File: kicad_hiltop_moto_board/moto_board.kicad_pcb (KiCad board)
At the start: 4 copper layers, 159.9 x 99.9 mm, 204 parts, among them J1 Conn_01x04, J10 Conn_01x01, J11 Conn_01x01, J12 Conn_01x03, J13 Conn_01x03, J2 Conn_01x04, J3 Conn_03x32_DIN41612, J4 Conn_01x04, J5 Conn_02x05_Top_Bottom, J6 Conn_01x01, J7 Conn_01x01, J8 Conn_01x03, J9 Conn_01x03, Q1 CSD18540Q5B, Q2 CSD18540Q5B, Q3 CSD18540Q5B, Q4 CSD18540Q5B, Q5 CSD18540Q5B, Q6 CSD18540Q5B, Q7 CSD18540Q5B, Q8 CSD18540Q5B, SW1 SW_Push, U1 DRV8704, U13 CP2102N-A01-GQFN24, U2 LD1117S33TR_SOT223, U22 STM32F072RBTx, U27 USB2502, U3 AT25DN512CSSHF-B, U7 DNF, Y1 50ppm 24.000MHZ, Y2 8MHZ, Y3 ABS25-32.768KHZ-6-T

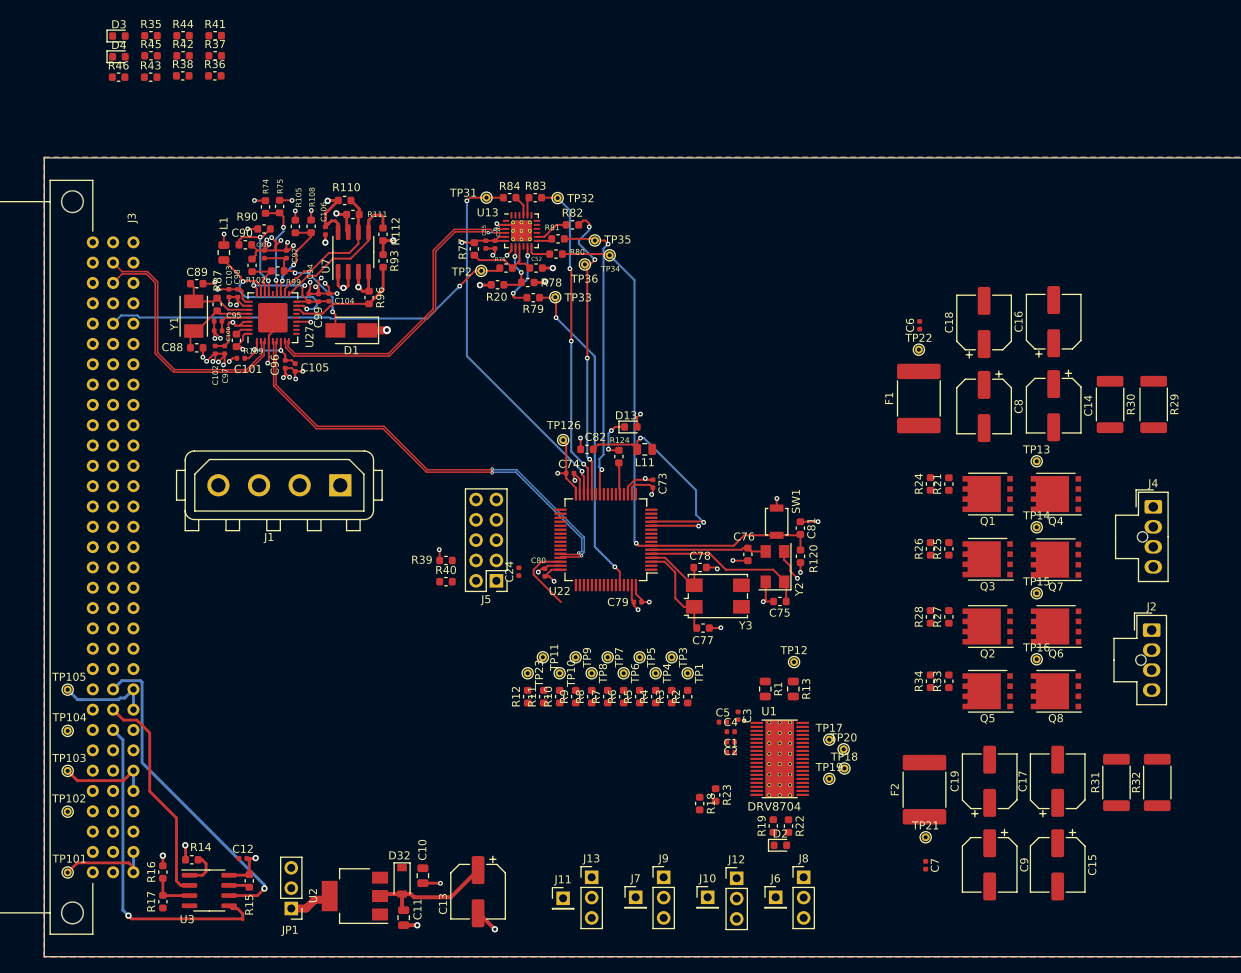
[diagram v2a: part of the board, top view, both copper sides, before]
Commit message: Updated moto board schematic and layout
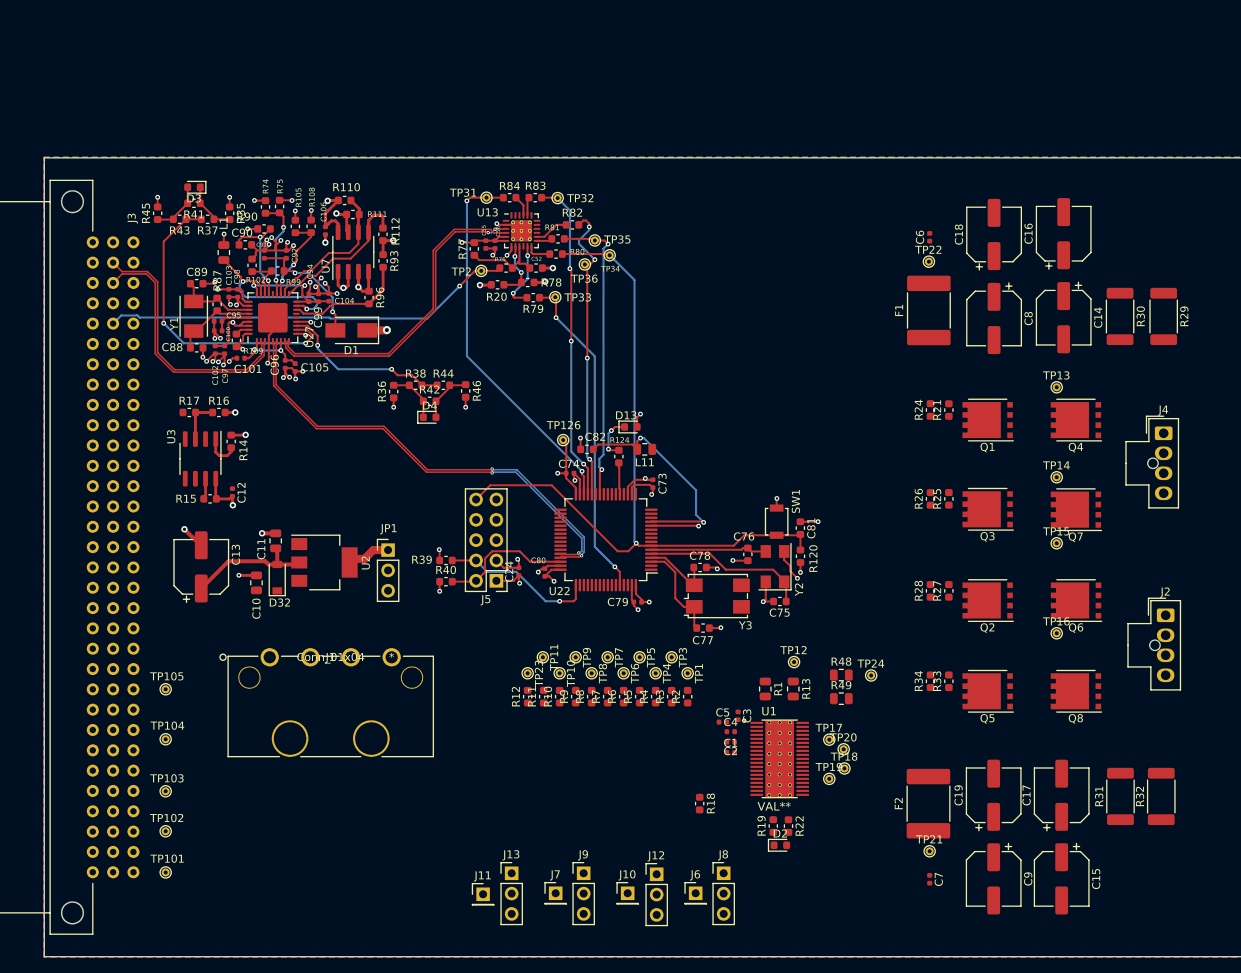
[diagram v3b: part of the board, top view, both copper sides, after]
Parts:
- removed R23: 10K, Resistor_SMD:R_0603_1608Metric
- added R48: DNF, Resistor_SMD:R_0805_2012Metric, F.Cu at (154.7, 109.7)
- added R49: 0R, Resistor_SMD:R_0805_2012Metric, F.Cu at (154.7, 112.7)
- added TP24: Test_Point, TestPoint:TestPoint_THTPad_D1.0mm_Drill0.5mm, F.Cu at (158.4, 109.8)
- J1: footprint Connector_TE-Connectivity:TE_MATE-N-LOK_350211-1_1x04_P5.08mm_Vertical -> Devtank_PCB_Lib:Molex_8981
- U1: value DRV8704 -> VAL**
- moved R17 61.2 mm to (73.2, 76.9), turned to 0 degrees
- moved D4 59.5 mm to (103.2, 77.5)
- moved R46 58.5 mm to (107.8, 74.2), turned to 270 degrees
- moved R16 57.9 mm to (76.9, 76.9), turned to 0 degrees
- moved R44 54.5 mm to (105.0, 73.5)
- moved U3 54.0 mm to (74.6, 82.7), turned to 270 degrees
- moved C13 53.3 mm to (74.7, 96.2), turned to 90 degrees
- moved R42 53.1 mm to (103.2, 75.5)
- moved R14 52.5 mm to (78.4, 80.5), turned to 90 degrees
- moved C11 49.7 mm to (84.0, 93.0), turned to 270 degrees
- moved R38 48.4 mm to (101.5, 73.5)
- moved R15 48.0 mm to (75.8, 87.7), turned to 0 degrees
- moved JP1 46.4 mm to (98.0, 94.1), turned to 0 degrees
- moved C12 45.8 mm to (78.6, 86.9), turned to 270 degrees
- moved R36 45.4 mm to (98.8, 74.3), turned to 90 degrees
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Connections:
- C14 pad 1: /motor_control/VM -> /motor_control/VM1
- C15 pad 1: /motor_control/VM -> /motor_control/VM2
- C16 pad 1: /motor_control/VM -> /motor_control/VM1
- C17 pad 1: /motor_control/VM -> /motor_control/VM2
- C18 pad 1: /motor_control/VM -> /motor_control/VM1
- C19 pad 1: /motor_control/VM -> /motor_control/VM2
- C4 pad 2: /motor_control/VM -> /VM
- C5 pad 1: /motor_control/VM -> /VM
- C6 pad 1: /motor_control/VM -> /motor_control/VM1
- C7 pad 1: /motor_control/VM -> /motor_control/VM2
- C8 pad 1: /motor_control/VM -> /motor_control/VM1
- C9 pad 1: /motor_control/VM -> /motor_control/VM2
- F1 pad 2: /motor_control/VM -> /motor_control/VM1
- F2 pad 1: /motor_control/VM -> /motor_control/VM2
- J1 pad 3: (no net) -> GND
- Q1 pad 1: Net-(Q1-Pad1) -> /motor_control/AOUT1
- Q1 pad 2: (no net) -> Net-(Q1-Pad2)
- Q1 pad 3: /AOUT1 -> Net-(F1-Pad1)
- Q2 pad 1: Net-(Q2-Pad1) -> /motor_control/BOUT1
- Q2 pad 2: (no net) -> Net-(Q2-Pad2)
- Q2 pad 3: /BOUT1 -> Net-(F2-Pad2)
- Q3 pad 1: Net-(Q3-Pad1) -> /motor_control/AOUT2
- Q3 pad 2: (no net) -> Net-(Q3-Pad2)
- Q3 pad 3: /AOUT2 -> Net-(F1-Pad1)
- Q4 pad 1: (no net) -> Net-(Q4-Pad1)
- Q4 pad 2: (no net) -> Net-(Q4-Pad2)
- Q4 pad 3: Net-(Q4-Pad3) -> /motor_control/AOUT1
- Q5 pad 1: Net-(Q5-Pad1) -> /motor_control/BOUT2
- Q5 pad 2: (no net) -> Net-(Q5-Pad2)
- Q5 pad 3: /BOUT2 -> Net-(F2-Pad2)
- Q6 pad 1: (no net) -> Net-(Q6-Pad1)
- Q6 pad 2: (no net) -> Net-(Q6-Pad2)
- Q6 pad 3: Net-(Q6-Pad3) -> /motor_control/BOUT1
- Q7 pad 1: (no net) -> Net-(Q4-Pad1)
- Q7 pad 2: (no net) -> Net-(Q7-Pad2)
- Q7 pad 3: Net-(Q4-Pad3) -> /motor_control/AOUT2
- Q8 pad 1: (no net) -> Net-(Q6-Pad1)
- Q8 pad 2: (no net) -> Net-(Q8-Pad2)
- Q8 pad 3: Net-(Q6-Pad3) -> /motor_control/BOUT2
- R1 pad 2: /motor_control/VM -> /VM
- R13 pad 2: /motor_control/VM -> /VM
- R21 pad 2: Net-(Q1-Pad4) -> Net-(Q1-Pad2)
- R24 pad 2: Net-(Q4-Pad4) -> Net-(Q4-Pad2)
- R25 pad 2: Net-(Q3-Pad4) -> Net-(Q3-Pad2)
- R26 pad 2: Net-(Q7-Pad4) -> Net-(Q7-Pad2)
- R27 pad 2: Net-(Q2-Pad4) -> Net-(Q2-Pad2)
- R28 pad 2: Net-(Q6-Pad4) -> Net-(Q6-Pad2)
- R29 pad 2: Net-(Q4-Pad3) -> Net-(Q4-Pad1)
- R30 pad 2: Net-(Q4-Pad3) -> Net-(Q4-Pad1)
- R31 pad 2: Net-(Q6-Pad3) -> Net-(Q6-Pad1)
- R32 pad 2: Net-(Q6-Pad3) -> Net-(Q6-Pad1)
- R33 pad 2: Net-(Q5-Pad4) -> Net-(Q5-Pad2)
- R34 pad 2: Net-(Q8-Pad4) -> Net-(Q8-Pad2)
- TP17 pad 1: Net-(Q4-Pad3) -> Net-(Q4-Pad1)
- TP18 pad 1: Net-(Q6-Pad3) -> Net-(Q6-Pad1)
- TP21 pad 1: /motor_control/VM -> /motor_control/VM2
- TP22 pad 1: /motor_control/VM -> /motor_control/VM1
- U1 pad 21: Net-(Q5-Pad1) -> /motor_control/BOUT2
- U1 pad 25: Net-(Q6-Pad3) -> Net-(Q6-Pad1)
- U1 pad 28: Net-(Q2-Pad1) -> /motor_control/BOUT1
- U1 pad 30: Net-(Q3-Pad1) -> /motor_control/AOUT2
- U1 pad 34: Net-(Q4-Pad3) -> Net-(Q4-Pad1)
- U1 pad 37: Net-(Q1-Pad1) -> /motor_control/AOUT1
- U1 pad 4: /motor_control/VM -> /VM
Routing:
- net /SPI0_MOSI: track 41.4 -> 0.00 mm, vias 1 -> 0
- net /SPI0_CLK: track 41.1 -> 0.00 mm, vias 1 -> 0
- net Net-(R37-Pad2): track 0.00 -> 38.4 mm, vias 0 -> 2
- net /SPI0_MISO: track 27.5 -> 0.00 mm
- net /STM_RESET: track 66.5 -> 91.1 mm
- net Net-(R38-Pad2): track 0.00 -> 21.6 mm, vias 0 -> 2
- net /SWD_SCK: track 0.00 -> 19.4 mm, vias 0 -> 1
- net ADJ_DC: track 12.1 -> 0.00 mm
- net +12V: track 12.1 -> 0.00 mm
- net -5V: track 11.8 -> 0.00 mm
- net GND: track 132.5 -> 140.4 mm, vias 56 -> 60
- net +3V3: track 83.4 -> 91.2 mm, vias 21 -> 25
- net /SWD_IO: track 9.21 -> 16.6 mm
- net Net-(D4-Pad2): track 0.00 -> 6.74 mm
- net Net-(D3-Pad2): track 0.00 -> 6.72 mm
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
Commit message: Moto board awaiting review
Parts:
- removed J10, J11: Conn_01x01, Connector_PinHeader_2.54mm:PinHeader_1x01_P2.54mm_Vertical
- removed J12, J13: Conn_01x03, Connector_PinHeader_2.54mm:PinHeader_1x03_P2.54mm_Vertical
- removed R4, R5, R6, R7: 0R, Resistor_SMD:R_0603_1608Metric
- removed R49: 0R, Resistor_SMD:R_0805_2012Metric
- added D5: GRN, LED_SMD:LED_0603_1608Metric, F.Cu at (143.0, 136.0)
- added G***: LOGO, Devtank_PCB_Lib:Devtank_Rev2_Logo_Small, F.Cu at (207.4, 121.1)
- added R23: 10K, Resistor_SMD:R_0603_1608Metric, F.Cu at (142.9, 133.7)
- added R47: 10K, Resistor_SMD:R_0603_1608Metric, F.Cu at (136.7, 131.4)
- added REF**: ESD-Logo_6.6x6mm_SilkScreen, Symbol:ESD-Logo_6.6x6mm_SilkScreen, F.Cu at (144.0, 53.0)
- added REF**: OSHW-Logo2_7.3x6mm_SilkScreen, Symbol:OSHW-Logo2_7.3x6mm_SilkScreen, F.Cu at (137.5, 77.0)
- added REF**: WEEE-Logo_4.2x6mm_SilkScreen, Symbol:WEEE-Logo_4.2x6mm_SilkScreen, F.Cu at (93.8, 83.3)
- added REF**: KiCad-Logo2_5mm_SilkScreen, Symbol:KiCad-Logo2_5mm_SilkScreen, F.Cu at (204.6, 64.2)
- added TP25: Test_Point, TestPoint:TestPoint_THTPad_D1.0mm_Drill0.5mm, F.Cu at (162.5, 113.5)
- added TP26: Test_Point, TestPoint:TestPoint_THTPad_D1.0mm_Drill0.5mm, F.Cu at (160.6, 136.7)
- added TP27: Test_Point, TestPoint:TestPoint_THTPad_D1.0mm_Drill0.5mm, F.Cu at (164.8, 90.8)
- added TP28: Test_Point, TestPoint:TestPoint_THTPad_D1.0mm_Drill0.5mm, F.Cu at (149.9, 104.5)
- added TP29: Test_Point, TestPoint:TestPoint_THTPad_D1.0mm_Drill0.5mm, F.Cu at (164.8, 102.2)
- added TP30: Test_Point, TestPoint:TestPoint_THTPad_D1.0mm_Drill0.5mm, F.Cu at (164.8, 113.5)
- added TP37: Test_Point, TestPoint:TestPoint_THTPad_D1.0mm_Drill0.5mm, F.Cu at (149.9, 131.4)
- added TP38: Test_Point, TestPoint:TestPoint_THTPad_D1.0mm_Drill0.5mm, F.Cu at (136.6, 134.6)
- J2, J4: footprint Connector_Molex:Molex_Nano-Fit_105309-xx04_1x04_P2.50mm_Vertical -> Devtank_PCB_Lib:Phoenix_Contact_SPTAF_4_way_terminal_block
- J6, J7: value Conn_01x01 -> Conn_01x04; footprint Connector_PinHeader_2.54mm:PinHeader_1x01_P2.54mm_Vertical -> Devtank_PCB_Lib:moto_board_4_pin_header
- J8, J9: value Conn_01x03 -> Conn_01x04; footprint Connector_PinHeader_2.54mm:PinHeader_1x03_P2.54mm_Vertical -> Devtank_PCB_Lib:moto_board_4_pin_header
- R1, R13: footprint Resistor_SMD:R_0805_2012Metric -> Resistor_SMD:R_1210_3225Metric
- R2: value 0R -> DNF
- R29, R30, R31, R32: value 0.5R -> 0.015R
- R48: footprint Resistor_SMD:R_0805_2012Metric -> Resistor_SMD:R_0603_1608Metric
- U1: value VAL** -> DRV8704
- moved R29 60.2 mm to (155.0, 109.9), turned to 180 degrees
- moved R30 52.5 mm to (155.0, 104.4), turned to 180 degrees
- moved TP18 42.5 mm to (162.5, 79.5)
- moved R32 40.2 mm to (155.0, 131.4), turned to 180 degrees
- moved TP17 40.0 mm to (164.8, 79.5)
- moved R31 36.6 mm to (155.0, 136.8), turned to 180 degrees
- moved TP19 33.3 mm to (162.5, 90.8)
- moved R48 26.9 mm to (138.8, 131.4), turned to 90 degrees
- moved J2 26.8 mm to (193.8, 129.0), turned to 270 degrees
- moved J8 19.8 mm to (120.3, 133.2)
- moved J4 18.5 mm to (194.0, 61.0), turned to 270 degrees
- moved J9 18.4 mm to (104.1, 133.2)
- moved TP20 15.4 mm to (160.3, 104.5), turned to 90 degrees
- moved Q4 12.6 mm to (196.6, 77.7)
- moved Q6 12.6 mm to (196.7, 100.4)
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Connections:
- C14 pad 1: /motor_control/VM1 -> /VM
- C15 pad 1: /motor_control/VM2 -> /VM
- C16 pad 1: /motor_control/VM1 -> /VM
- C17 pad 1: /motor_control/VM2 -> /VM
- C18 pad 1: /motor_control/VM1 -> /VM
- C19 pad 1: /motor_control/VM2 -> /VM
- C6 pad 1: /motor_control/VM1 -> /VM
- C7 pad 1: /motor_control/VM2 -> /VM
- C8 pad 1: /motor_control/VM1 -> /VM
- C9 pad 1: /motor_control/VM2 -> /VM
- F1 pad 2: /motor_control/VM1 -> /VM
- F2 pad 1: /motor_control/VM2 -> /VM
- J2 pad 1: /BOUT1 -> /B1
- J2 pad 2: /BOUT2 -> /B2
- J2 pad 4: (no net) -> Net-(J2-Pad4)
- J4 pad 1: /AOUT1 -> /A1
- J4 pad 2: /AOUT2 -> /A2
- J4 pad 4: (no net) -> Net-(J4-Pad4)
- J6 pad 1: (no net) -> /V5
- J7 pad 1: (no net) -> /V5
- J8 pad 2: /M_AIN1 -> /M_AIN2
- J9 pad 2: /M_BIN1 -> /M_BIN2
- Q1 pad 1: /motor_control/AOUT1 -> /A1
- Q2 pad 1: /motor_control/BOUT1 -> /B1
- Q3 pad 1: /motor_control/AOUT2 -> /A2
- Q4 pad 3: /motor_control/AOUT1 -> /A1
- Q5 pad 1: /motor_control/BOUT2 -> /B2
- Q6 pad 3: /motor_control/BOUT1 -> /B1
- Q7 pad 3: /motor_control/AOUT2 -> /A2
- Q8 pad 3: /motor_control/BOUT2 -> /B2
- R48 pad 1: ADJ_DC -> GND
- R48 pad 2: /VM -> /motor_control/SLEEPn
- TP13 pad 1: /AOUT1 -> /A1
- TP14 pad 1: /AOUT2 -> /A2
- TP15 pad 1: /BOUT1 -> /B1
- TP16 pad 1: /BOUT2 -> /B2
- TP17 pad 1: Net-(Q4-Pad1) -> Net-(R21-Pad1)
- TP18 pad 1: Net-(Q6-Pad1) -> Net-(R24-Pad1)
- TP19 pad 1: GND -> Net-(R26-Pad1)
- TP21 pad 1: /motor_control/VM2 -> /VM
- TP22 pad 1: /motor_control/VM1 -> /VM
- TP24 pad 1: /12V_EXT -> Net-(R28-Pad1)
- U1 pad 10: /motor_control/AIN1 -> /M_AIN1
- U1 pad 11: /motor_control/AIN2 -> /M_AIN2
- U1 pad 12: /motor_control/BIN1 -> /M_BIN1
- U1 pad 13: /motor_control/BIN2 -> /M_BIN2
- U1 pad 21: /motor_control/BOUT2 -> /B2
- U1 pad 28: /motor_control/BOUT1 -> /B1
- U1 pad 30: /motor_control/AOUT2 -> /A2
- U1 pad 37: /motor_control/AOUT1 -> /A1
- U22 pad 10: (no net) -> /M_RESET
- U22 pad 11: (no net) -> /M_SLEEPn
- U22 pad 22: (no net) -> /PWM_1
- U22 pad 34: /M_BIN2 -> (no net)
- U22 pad 35: /M_SLEEPn -> /PWM_2
- U22 pad 36: /M_RESET -> (no net)
- U22 pad 38: /M_FAULTn -> (no net)
- U22 pad 39: /M_SCS -> (no net)
- U22 pad 40: /M_AIN2 -> (no net)
- U22 pad 41: /M_AIN1 -> (no net)
- U22 pad 42: /M_BIN1 -> (no net)
- U22 pad 53: (no net) -> /M_FAULTn
- U22 pad 54: (no net) -> /M_SCS
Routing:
- net /A1: track 0.00 -> 110.6 mm, vias 0 -> 1
- net /A2: track 0.00 -> 103.2 mm, vias 0 -> 2
- net +5V: track 26.2 -> 124.2 mm, vias 2 -> 4
- net Net-(Q4-Pad1): track 0.00 -> 92.8 mm, vias 0 -> 4
- net ADJ_DC: track 0.00 -> 87.8 mm, vias 0 -> 2
- net Net-(Q6-Pad1): track 0.00 -> 81.9 mm, vias 0 -> 3
- net /B1: track 0.00 -> 78.1 mm, vias 0 -> 1
- net /V5: track 0.00 -> 71.1 mm, vias 0 -> 2
- net /B2: track 0.00 -> 69.4 mm, vias 0 -> 1
- net /M_BIN2: track 0.00 -> 67.9 mm
- net /12V_EXT: track 0.00 -> 66.3 mm
- net /PWM_2: track 0.00 -> 64.7 mm, vias 0 -> 2
- net /PWM_1: track 0.00 -> 63.3 mm, vias 0 -> 1
- net /M_AIN2: track 0.00 -> 59.6 mm
- net /M_BIN1: track 0.00 -> 59.4 mm
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- added copper zone on F.Cu, net /A1
- added copper zone on F.Cu, net /A2
- added copper zone on F.Cu, net /B1
- added copper zone on F.Cu, net /B2
- added copper zone on F.Cu, net /VM
- added copper zone on In2.Cu, net /VM
- added copper zone on F.Cu, net Net-(F1-Pad1)
- added copper zone on In2.Cu, net Net-(F1-Pad1)
- added copper zone on F.Cu, net Net-(F2-Pad2)
- added copper zone on In2.Cu, net Net-(F2-Pad2)
- added copper zone on F.Cu, net Net-(Q4-Pad1)
- added copper zone on F.Cu, net Net-(Q6-Pad1)
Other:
- board text added: "AIN1"
- board text added: "AIN2"
- board text added: "BIN1"
- board text added: "BIN2"
- board text added: "Direct PWM Jumper settings"
- board text added: "HIGH"
- board text added: "LOW"
- board text added: "Licensed under CERN OHL v1.2"
- board text added: "Moto Board"
- board text added: "Motor x output Full speed forward current Brake, low-side slow decay Coast, h-bridge disabled Full speed reverse current Reverse current + slow decay Forward current + slow decay Reverse current + fast decay Forward current + fast decay No output Ext controller connected"
- board text added: "PN: 304-008"
- board text added: "PWM"
- board text added: "Rev: A"
- board text added: "xIN1 HIGH HIGH LOW LOW HIGH PWM LOW PWM PWM N/A"
- board text added: "xIN2 LOW HIGH LOW HIGH PWM HIGH PWM LOW PWM N/A"

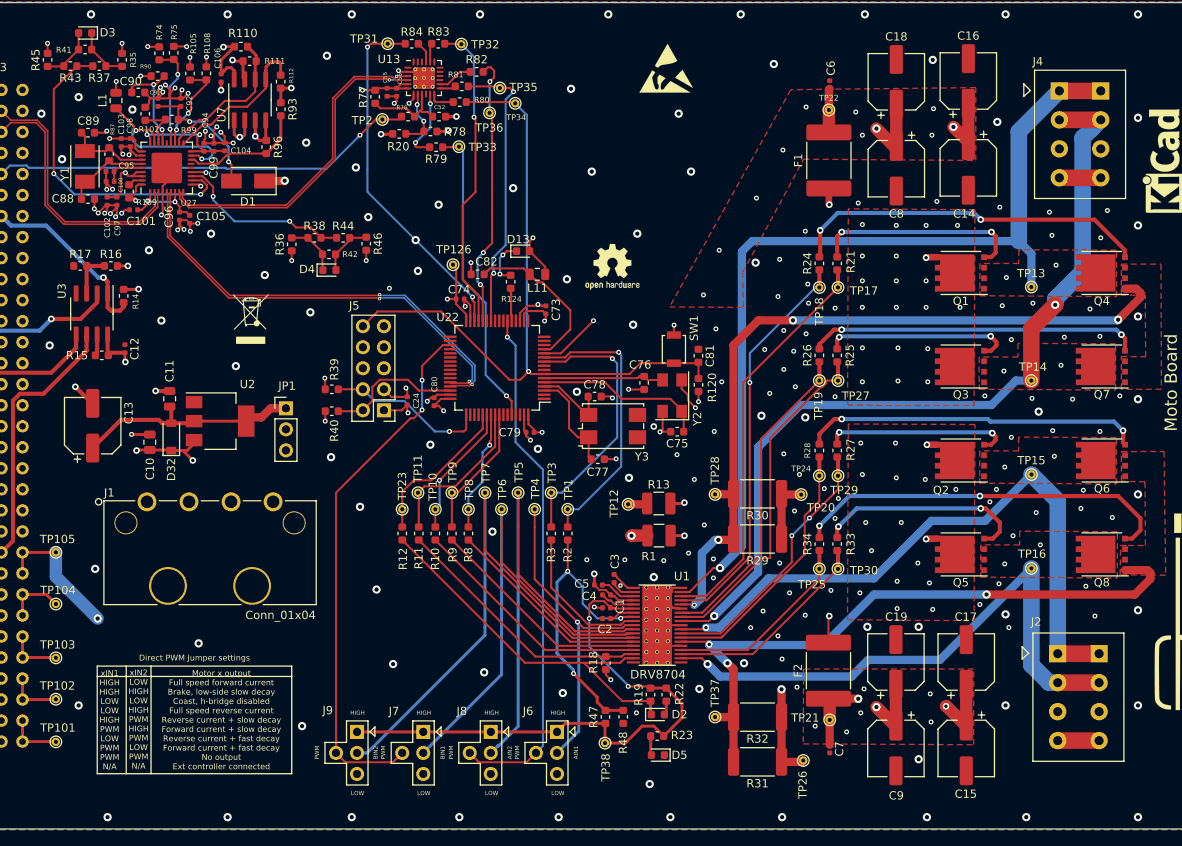
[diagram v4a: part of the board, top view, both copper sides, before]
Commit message: Moto board connectors moved
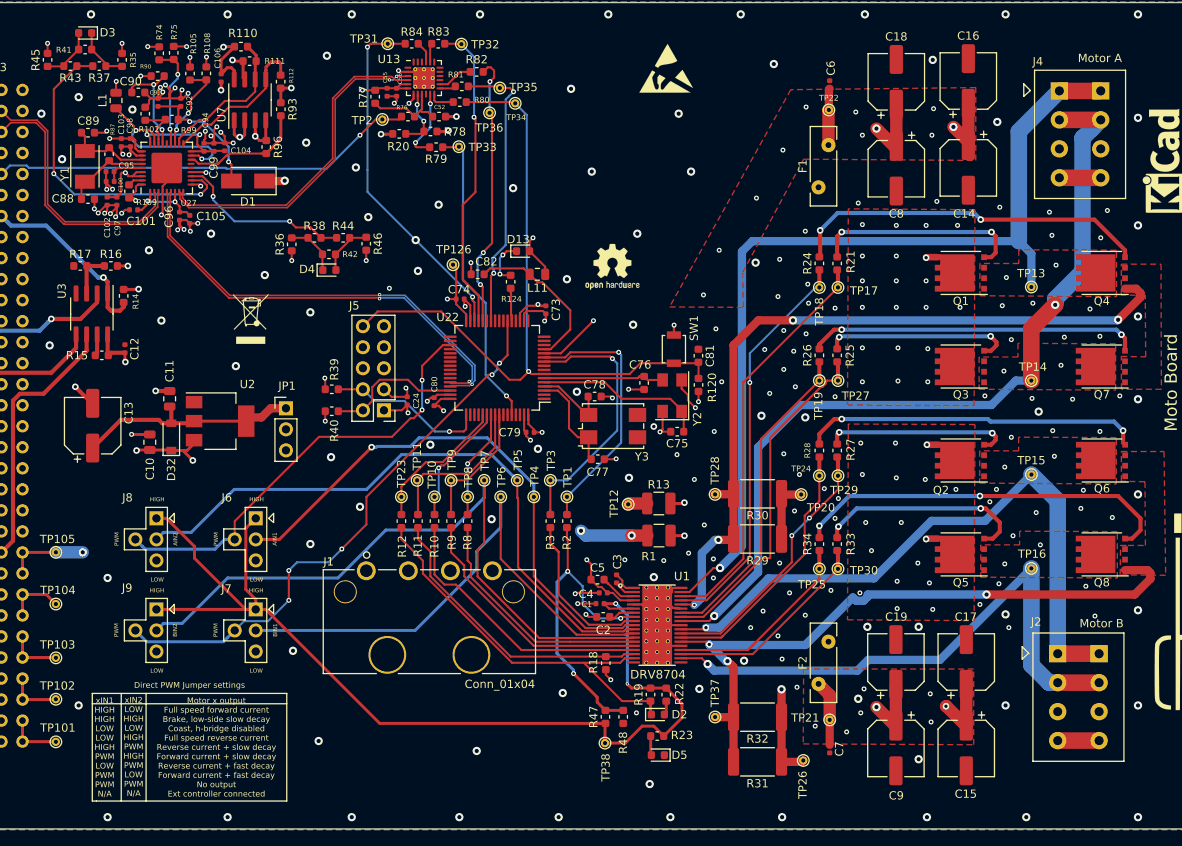
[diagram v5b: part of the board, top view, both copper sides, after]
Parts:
- C1, C5: footprint Capacitor_SMD:C_0402_1005Metric -> Capacitor_SMD:C_0603_1608Metric
- D2: value LED -> RED
- F1, F2: footprint Fuse:Fuse_2920_7451Metric -> Fuse:Fuse_Bourns_MF-RHT200
- moved J8 47.9 mm to (79.9, 107.4)
- moved J6 44.6 mm to (91.9, 107.4)
- moved J9 28.4 mm to (79.9, 118.4)
- moved J1 27.8 mm to (123.0, 113.7)
- moved J7 25.1 mm to (91.9, 118.4)
- moved F1 3.48 mm to (162.4, 67.4)
- moved F2 2.00 mm to (162.4, 127.4)
- moved R10 1.50 mm to (116.0, 107.7)
- moved R11 1.50 mm to (114.0, 107.7)
- moved R12 1.50 mm to (112.0, 107.7)
- moved R2 1.50 mm to (132.0, 107.7)
- moved R3 1.50 mm to (130.0, 107.7)
- moved R8 1.50 mm to (120.0, 107.7)
- moved R9 1.50 mm to (118.0, 107.7)
- moved TP1 1.50 mm to (132.0, 104.8)
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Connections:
- U22 pad 22: /PWM_1 -> /PWM_2
- U22 pad 35: /PWM_2 -> /PWM_1
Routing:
- net /V5: track 71.1 -> 128.1 mm
- net /12V_EXT: track 66.3 -> 37.3 mm
- net /M_AIN1: track 39.9 -> 66.9 mm
- net /M_AIN2: track 59.6 -> 76.9 mm
- net /M_BIN2: track 67.9 -> 82.3 mm
- net /PWM_1: track 63.3 -> 53.1 mm, vias 1 -> 2
- net /M_BIN1: track 59.4 -> 67.1 mm
- net ADJ_DC: track 87.8 -> 82.1 mm, vias 2 -> 3
- net /motor_control/SCS: track 29.4 -> 33.5 mm
- net /motor_control/SCLK: track 25.0 -> 29.0 mm
- net /PWM_2: track 64.7 -> 68.4 mm, vias 2 -> 5
- net /motor_control/SDATO: track 31.9 -> 35.2 mm
- net GND: track 183.6 -> 186.9 mm, vias 153 -> 154
- net Net-(F2-Pad2): track 6.87 -> 3.62 mm, vias 47 -> 46
- net /motor_control/SDATI: track 27.2 -> 30.5 mm
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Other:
- board text added: "Motor A"
- board text added: "Motor B"
